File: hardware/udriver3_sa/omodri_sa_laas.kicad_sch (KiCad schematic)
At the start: 17 parts, among them J2 DF13_01x05_THT, J4 Conn_01x11

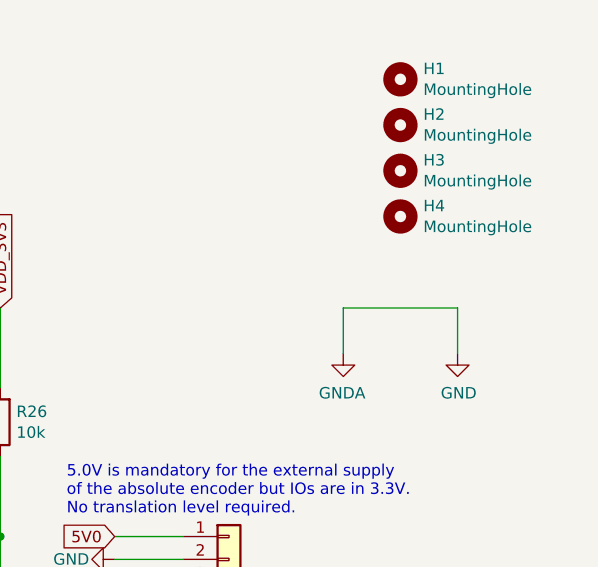
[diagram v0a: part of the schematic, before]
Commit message: Third release of uOmodri Single Axis (uOmodri_SA). Add Test points.
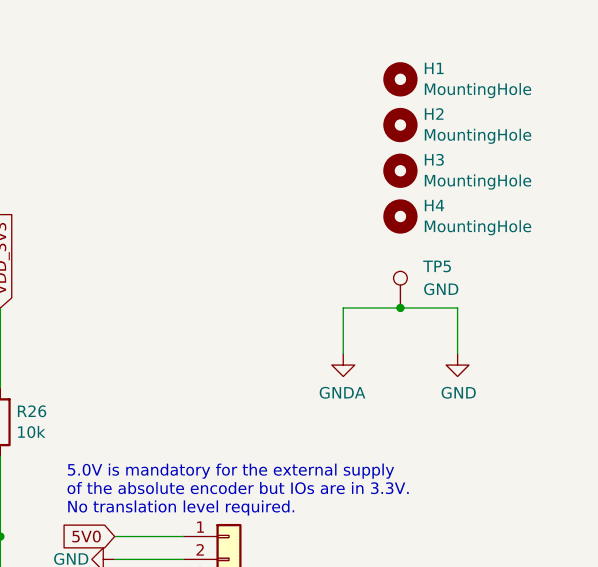
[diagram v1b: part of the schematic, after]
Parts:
- added TP5: GND, TestPoint:TestPoint_Keystone_5019_Minature, symbol Connector:TestPoint
- G1: Manufacturer (none) -> LAAS
- G2: Manufacturer (none) -> OSHWA
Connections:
- net GND: now also TP5.1
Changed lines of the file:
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@@
+	)
+	(junction
+		(at 260.35 50.8)
+		(diameter 0)
+		(color 0 0 0 0)
 	)
 	(junction
@@
 	(wire
 		(pts
-			(xy 254 50.8) (xy 266.7 50.8)
+			(xy 254 50.8) (xy 260.35 50.8)
 		)
 		(stroke
@@
 		(pts
 			(xy 194.31 91.44) (xy 236.22 91.44)
+		)
+		(stroke
+			(width 0)
+			(type default)
+		)
+	)
+	(wire
+		(pts
+			(xy 260.35 50.8) (xy 266.7 50.8)
 		)
 		(stroke
@@
 			)
 		)
-		(property "Datasheet" ""
+		(property "Datasheet" "https://www.laas.fr/fr/"
 			(at 266.7 101.6 0)
 			(effects
@@
 			)
 		)
-		(property "Description" ""
+		(property "Description" "LAAS logo"
 			(at 266.7 101.6 0)
 			(effects
@@
 			)
 		)
-		(property "Manufacturer" ""
+		(property "Manufacturer" "LAAS"
 			(at 266.7 101.6 0)
 			(effects
@@
 			)
 		)
-		(property "Datasheet" ""
+		(property "Datasheet" "https://www.oshwa.org/"
 			(at 266.7 114.3 0)
 			(effects
@@
 			)
 		)
-		(property "Description" ""
+		(property "Description" "Open Hardware logo"
 			(at 266.7 114.3 0)
 			(effects
@@
 			)
 		)
-		(property "Manufacturer" ""
+		(property "Manufacturer" "OSHWA"
 			(at 266.7 114.3 0)
 			(effects
@@
 					(unit 1)
 				)
+			)
+		)
+	)
+	(symbol
+		(lib_id "Connector:TestPoint")
+		(at 260.35 50.8 0)
+		(unit 1)
+		(exclude_from_sim no)
+		(in_bom yes)
+		(on_board yes)
+		(dnp no)
+		(fields_autoplaced yes)
+		(property "Reference" "TP5"
+			(at 262.89 46.2279 0)
+			(effects
+				(font
+					(size 1.27 1.27)
+				)
+				(justify left)
+			)
+		)
+		(property "Value" "GND"
+			(at 262.89 48.7679 0)
+			(effects
+				(font
+					(size 1.27 1.27)
+				)
+				(justify left)
+			)
+		)
+		(property "Footprint" "TestPoint:TestPoint_Keystone_5019_Minature"
+			(at 265.43 50.8 0)
+			(effects
+				(font
+					(size 1.27 1.27)
+				)
+				(hide yes)
+			)
+		)
+		(property "Datasheet" "https://www.keyelco.com/product.cfm/Miniature/5019/product_id/1357"
+			(at 265.43 50.8 0)
+			(effects
+				(font
+					(size 1.27 1.27)
+				)
+				(hide yes)
+			)
+		)
+		(property "Description" "test point"
+			(at 260.35 50.8 0)
+			(effects
+				(font
+					(size 1.27 1.27)
+				)
+				(hide yes)
+			)
+		)
+		(property "Assembling" "SMD"
+			(at 260.35 50.8 0)
+			(effects
+				(font
+					(size 1.27 1.27)
+				)
+				(hide yes)
+			)
+		)
+		(property "DigiKey" "36-5019CT-ND"
+			(at 260.35 50.8 0)
+			(effects
+				(font
+					(size 1.27 1.27)
+				)
+				(hide yes)
+			)
+		)
+		(property "Farnell" "2529475"
+			(at 260.35 50.8 0)
+			(effects
+				(font
+					(size 1.27 1.27)
+				)
+				(hide yes)
+			)
+		)
+		(property "Mouser" "534-5019"
+			(at 260.35 50.8 0)
+			(effects
+				(font
+					(size 1.27 1.27)
+				)
+				(hide yes)
+			)
+		)
+		(property "Manufacturer" "KEYSTONE"
+			(at 260.35 50.8 0)
+			(effects
+				(font
+					(size 1.27 1.27)
+				)
+				(hide yes)
+			)
+		)
+		(property "Part No" "5019"
+			(at 260.35 50.8 0)
+			(effects
+				(font
+					(size 1.27 1.27)
+				)
+				(hide yes)
+			)
+		)
+		(pin "1"
+		)
+		(instances
+			(project "omodri_sa_laas"
+				(path "/de5b13f0-933a-4c4d-9979-13dc57b13241"
+					(reference "TP5")
+					(unit 1)
+				)

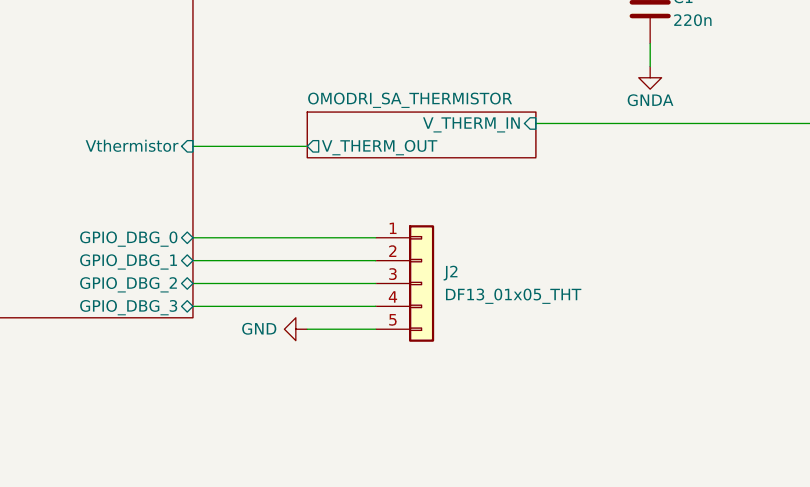
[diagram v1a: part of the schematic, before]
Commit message: Update of the multicolor led footprints in uOmodri V3.1 & uOmodri_SA V1.0.
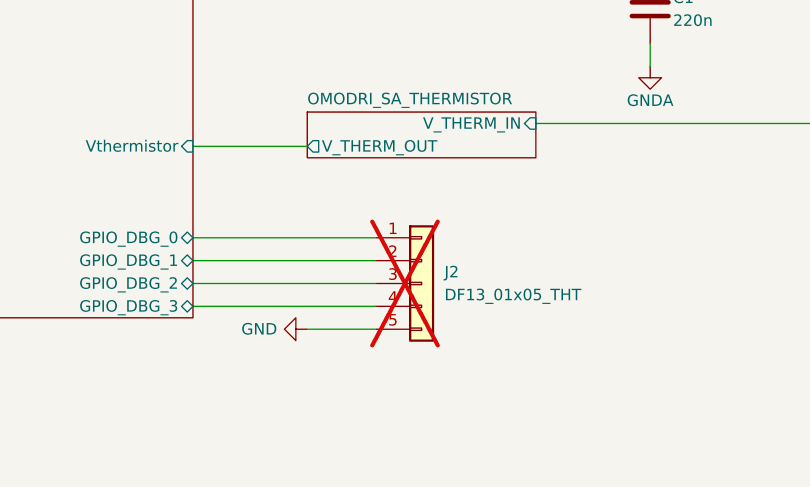
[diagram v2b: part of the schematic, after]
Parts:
- J2: now not fitted
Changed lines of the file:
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@@
 		(in_bom yes)
 		(on_board yes)
-		(dnp no)
+		(dnp yes)
 		(fields_autoplaced yes)
 		(property "Reference" "J2"

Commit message: Update some reference on uOmodri V3.1 for fab. Update uOmodri_SA V1.0 reducing heights of top layers components.
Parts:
- H1, H2, H3, H4: footprint MountingHole:MountingHole_2.2mm_M2 -> MountingHole:MountingHole_2.2mm_M2_ISO7380_Pad_TopBottom
- TP5: footprint TestPoint:TestPoint_Keystone_5019_Minature -> TestPoint:TestPoint_Keystone_5015_Micro-Minature; DigiKey 36-5019CT-ND -> 36-5015CT-ND; Farnell 2529475 -> 3858030; LCSC (none) -> C2906768; Mouser 534-5019 -> 534-5015; Part No 5019 -> 5015
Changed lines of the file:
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@@
 			)
 		)
-		(property "Footprint" "MountingHole:MountingHole_2.2mm_M2"
+		(property "Footprint" "MountingHole:MountingHole_2.2mm_M2_ISO7380_Pad_TopBottom"
 			(at 260.35 25.4 0)
 			(effects
@@
 			)
 		)
-		(property "Footprint" "MountingHole:MountingHole_2.2mm_M2"
+		(property "Footprint" "MountingHole:MountingHole_2.2mm_M2_ISO7380_Pad_TopBottom"
 			(at 260.35 30.48 0)
 			(effects
@@
 			)
 		)
-		(property "Footprint" "MountingHole:MountingHole_2.2mm_M2"
+		(property "Footprint" "MountingHole:MountingHole_2.2mm_M2_ISO7380_Pad_TopBottom"
 			(at 260.35 35.56 0)
 			(effects
@@
 			)
 		)
-		(property "Footprint" "MountingHole:MountingHole_2.2mm_M2"
+		(property "Footprint" "MountingHole:MountingHole_2.2mm_M2_ISO7380_Pad_TopBottom"
 			(at 260.35 40.64 0)
 			(effects
@@
 			)
 		)
-		(property "Footprint" "TestPoint:TestPoint_Keystone_5019_Minature"
+		(property "Footprint" "TestPoint:TestPoint_Keystone_5015_Micro-Minature"
 			(at 265.43 50.8 0)
 			(effects
@@
 			)
 		)
-		(property "Datasheet" "https://www.keyelco.com/product.cfm/Miniature/5019/product_id/1357"
+		(property "Datasheet" "https://www.keyelco.com/product.cfm/Micro-Miniature/5015/product_id/1353"
 			(at 265.43 50.8 0)
 			(effects
@@
 			)
 		)
-		(property "DigiKey" "36-5019CT-ND"
+		(property "DigiKey" "36-5015CT-ND "
 			(at 260.35 50.8 0)
 			(effects
@@
 			)
 		)
-		(property "Farnell" "2529475"
+		(property "Farnell" "3858030"
 			(at 260.35 50.8 0)
 			(effects
@@
 			)
 		)
-		(property "Mouser" "534-5019"
+		(property "Mouser" "534-5015"
 			(at 260.35 50.8 0)
 			(effects
@@
 			)
 		)
-		(property "Part No" "5019"
+		(property "Part No" "5015"
 			(at 260.35 50.8 0)
 			(effects
+				(font
+					(size 1.27 1.27)
+				)
+				(hide yes)
+			)
+		)
+		(property "LCSC" "C2906768"
+			(at 260.35 50.8 0)
+			(effects

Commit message: Update on uOmodri_SA. Remove USB, com SPI & debug connectors for integration into Myactuator motors. Connectors replaced by a ZIF connector.
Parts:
- removed H2, H3, H4: MountingHole, MountingHole:MountingHole_2.2mm_M2_ISO7380_Pad_TopBottom, symbol Mechanical:MountingHole
- removed J2: DF13_01x05_THT, udriver3:Hirose_DF13-05P-1.25DSA_1x05_P1.25mm_Vertical, symbol Connector_Generic:Conn_01x05
- removed R2, R3: 10k, Resistor_SMD:R_0201_0603Metric, symbol Device:R
- added H2, H3, H4: MountingHole, MountingHole:MountingHole_2.2mm_M2_ISO14580_Pad_TopBottom, symbol Mechanical:MountingHole_Pad
- added J2: conn_01x20_MountingPins, udriver3:Molex_FBH1_FFC_FPC_503480-2000_1x20-2MP_P0.50mm_Horizontal, symbol omodri_lib:conn_01x20_MountingPins
- added R5, R7: 10, Resistor_SMD:R_0201_0603Metric, symbol Device:R
- added R6, R8, R9: 10k, Resistor_SMD:R_0201_0603Metric, symbol Device:R
- H1: footprint MountingHole:MountingHole_2.2mm_M2_ISO7380_Pad_TopBottom -> MountingHole:MountingHole_2.2mm_M2_ISO14580_Pad_TopBottom; symbol Mechanical:MountingHole -> Mechanical:MountingHole_Pad
- J1: renamed from J4; Assembling SMD -> (none)
- renumbered R26 to R1, R28 to R2, R27 to R3, R1 to R4, TP5 to TP1
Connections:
- net GND: now also J2.1 (Pin_1), J2.10 (Pin_10), J2.13 (Pin_13), J2.17 (Pin_17), J2.20 (Pin_20), J2.6 (Pin_6), J2.8 (Pin_8), J2.MP1 (MountPin1), J2.MP2 (MountPin2)
- net OMODRI_SA_MCU/GPIO_DBG_0: now also J2.5 (Pin_5)
- net OMODRI_SA_MCU/GPIO_DBG_1: now also J2.4 (Pin_4)
- net OMODRI_SA_MCU/GPIO_DBG_2: now also J2.3 (Pin_3)
- net OMODRI_SA_MCU/GPIO_DBG_3: now also J2.2 (Pin_2)
- net OMODRI_SA_MCU/GPIO_SELECT_0: now also R8.2
- net OMODRI_SA_MCU/GPIO_SELECT_1: now also R9.2
- net OMODRI_SA_MCU/USB_N: now also J2.14 (Pin_14)
- net OMODRI_SA_MCU/USB_P: now also J2.15 (Pin_15)
- net VDD_3V3: now also R6.1, R8.1, R9.1
- new net COM_SIMO: J2.12 (Pin_12), R5.2
- new net COM_SOMI: J2.7 (Pin_7), R7.2
- new net OMODRI_SA_CAN_RS485/CAN_RS485_N: J2.19 (Pin_19)
- new net OMODRI_SA_CAN_RS485/CAN_RS485_P: J2.18 (Pin_18)
- new net OMODRI_SA_MCU/COM_SPI_CLK: J2.9 (Pin_9)
- new net OMODRI_SA_MCU/COM_SPI_SIMO: R5.1
- new net OMODRI_SA_MCU/COM_SPI_SOMI: R7.1
- new net OMODRI_SA_MCU/~{COM_SPI_CSn}: J2.11 (Pin_11), R6.2
- new net OMODRI_SA_USB/Vbus: J2.16 (Pin_16)
- no-connect marks 0 -> 4
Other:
- removed sheet OMODRI_SA_COM_SPI
- sheet OMODRI_SA_CAN_RS485 ports: added CAN_RS485_N, CAN_RS485_P, RS485_RX, RS485_TX, RS485_TX_EN; removed SCI_RX, SCI_TX, SCI_TX_EN
- sheet OMODRI_SA_USB ports: added Vbus; removed none
- moved on the sheet: G1, G2, TP1
